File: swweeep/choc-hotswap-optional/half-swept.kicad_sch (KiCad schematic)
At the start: 31 parts, among them J1 JST-BATTERY, SW1 SW_Push, SW10 SW_Push, SW11 SW_Push, SW12 SW_Push, SW14 SW_Push, SW15 SW_Push, SW16 SW_Push, SW17 SW_Push, SW18 SW_Push, SW2 SW_Push, SW20 SW_Push, SW21 SW_Push, SW3 SW_Push, SW4 SW_Push, SW5 SW_Push, SW6 SW_Push, SW7 SW_DPDT, SW8 SW_Push, SW9 SW_Push, U1 nice_nano

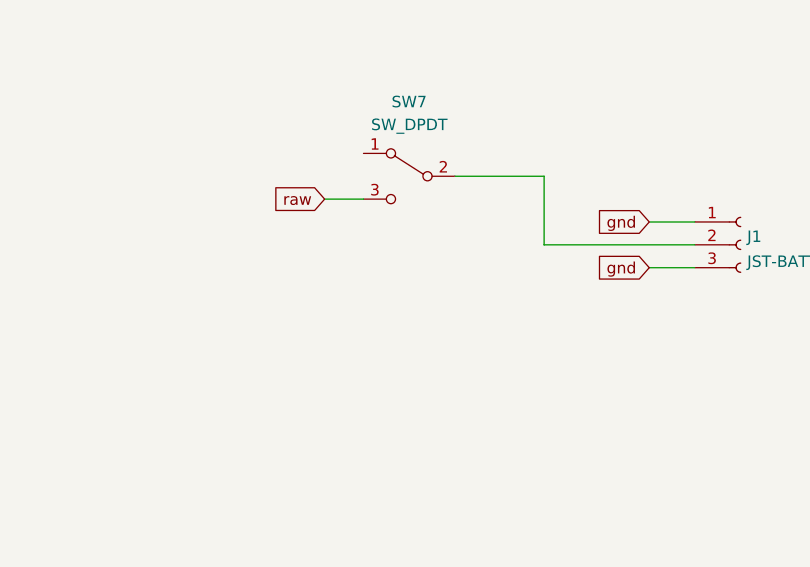
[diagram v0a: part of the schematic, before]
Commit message: Revert "replaced on off switch, from MSK12C02 to OS102011MA1QN1"
This reverts commit 761ca253cc3f7c0a016fc91ec44eaa0a86f70d5a.
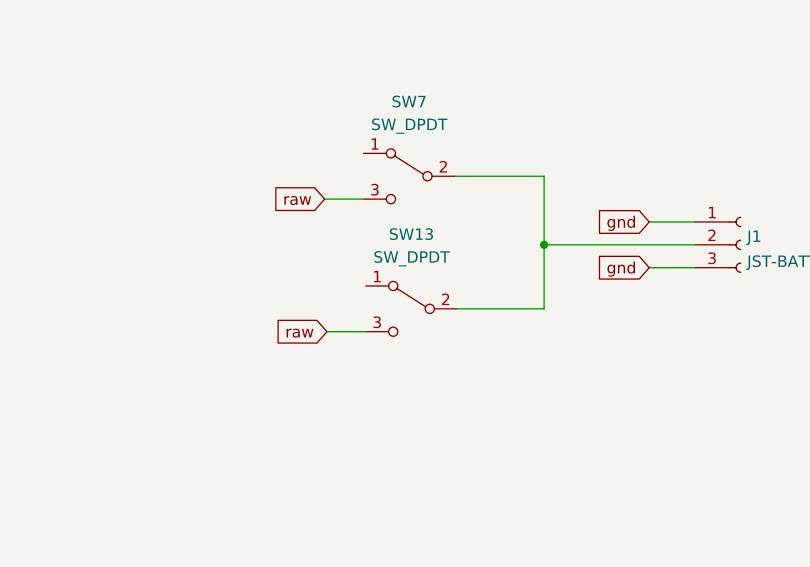
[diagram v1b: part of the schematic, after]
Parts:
- added SW13: SW_DPDT, fingerpunch:MSK-12C02, symbol jiran-ble:SW_DPDT
- SW7: footprint fingerpunch:SW_CuK_OS102011MA1QN1_SPDT_Angled -> fingerpunch:MSK-12C02
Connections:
- net raw: now also SW13.3 (C)
- net at J1.2 (Pin_2), SW7.2 (B): now also SW13.2 (B)
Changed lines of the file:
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@@
   (junction (at 66.548 143.764) (diameter 0) (color 0 0 0 0)
   )
+  (junction (at 175.26 121.158) (diameter 0) (color 0 0 0 0)
+  )
   (junction (at 100.33 143.764) (diameter 0) (color 0 0 0 0)
   )
@@
   (junction (at 90.17 133.604) (diameter 0) (color 0 0 0 0)
   )
+  (wire (pts (xy 151.13 130.81) (xy 155.448 130.81))
+    (stroke (width 0) (type default) (color 0 0 0 0))
+  )
   (wire (pts (xy 100.33 143.764) (xy 100.33 162.814))
     (stroke (width 0) (type default) (color 0 0 0 0))
@@
     (stroke (width 0) (type default) (color 0 0 0 0))
   )
+  (wire (pts (xy 175.26 121.158) (xy 175.26 128.27))
+    (stroke (width 0) (type default) (color 0 0 0 0))
+  )
   (wire (pts (xy 81.534 141.224) (xy 97.79 141.224))
     (stroke (width 0) (type default) (color 0 0 0 0))
@@
   )
   (wire (pts (xy 53.34 136.144) (xy 59.436 136.144))
+    (stroke (width 0) (type default) (color 0 0 0 0))
+  )
+  (wire (pts (xy 175.26 128.27) (xy 165.608 128.27))
     (stroke (width 0) (type default) (color 0 0 0 0))
   )
@@
     (effects (font (size 1.27 1.27)) (justify right))
     (property "Intersheet References" "${INTERSHEET_REFS}" (id 0) (at 0 0 0)
+      (effects (font (size 1.27 1.27)) hide)
+    )
+  )
+  (global_label "raw" (shape input) (at 151.13 130.81 180) (fields_autoplaced)
+    (effects (font (size 1.27 1.27)) (justify right))
+    (property "Intersheet References" "${INTERSHEET_REFS}" (id 0) (at 345.44 166.37 0)
       (effects (font (size 1.27 1.27)) hide)
     )
@@
     (property "Reference" "SW7" (id 0) (at 160.274 105.283 0))
     (property "Value" "SW_DPDT" (id 1) (at 160.274 107.823 0))
-    (property "Footprint" "fingerpunch:SW_CuK_OS102011MA1QN1_SPDT_Angled" (id 2) (at 158.369 105.918 0)
+    (property "Footprint" "fingerpunch:MSK-12C02" (id 2) (at 158.369 105.918 0)
       (effects (font (size 1.27 1.27)) hide)
     )
@@
     )
     (property "LCSC" "C431540" (id 4) (at 159.004 113.538 0)
+      (effects (font (size 1.27 1.27)) hide)
+    )
+    (pin "1")
+    (pin "2")
+    (pin "3")
+  )
+  (symbol (lib_id "jiran-ble:SW_DPDT") (at 159.258 128.27 0) (mirror y) (unit 1)
+    (in_bom yes) (on_board yes)
+    (property "Reference" "SW13" (id 0) (at 160.528 120.015 0))
+    (property "Value" "SW_DPDT" (id 1) (at 160.528 122.555 0))
+    (property "Footprint" "fingerpunch:MSK-12C02" (id 2) (at 158.623 120.65 0)
+      (effects (font (size 1.27 1.27)) hide)
+    )
+    (property "Datasheet" "" (id 3) (at 158.623 120.65 0)
+      (effects (font (size 1.27 1.27)) hide)
+    )
+    (property "LCSC" "C431540" (id 4) (at 159.258 128.27 0)
       (effects (font (size 1.27 1.27)) hide)
     )
@@
     )
     (path "/764570c2-a63f-40d9-bd89-9de3cab3ff49"
-      (reference "SW7") (unit 1) (value "SW_DPDT") (footprint "fingerpunch:SW_CuK_OS102011MA1QN1_SPDT_Angled")
+      (reference "SW7") (unit 1) (value "SW_DPDT") (footprint "fingerpunch:MSK-12C02")
     )
     (path "/00000000-0000-0000-0000-0000604a6c6c"
@@
       (reference "SW12") (unit 1) (value "SW_Push") (footprint "fingerpunch:Kailh_socket_PG1350_optional_reversible_millmax")
     )
+    (path "/86051a60-18a2-4d3f-bde8-435d97aaaf3f"
+      (reference "SW13") (unit 1) (value "SW_DPDT") (footprint "fingerpunch:MSK-12C02")
+    )
     (path "/00000000-0000-0000-0000-0000604bad64"
